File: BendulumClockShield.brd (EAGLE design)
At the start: 53.3 x 59.7 mm, 25 parts, among them J1 Cold Start, P1 Clock, P2 IR Recv, P3 Coil, P4 Batt, P5 Pwr, U1 LP2951-N

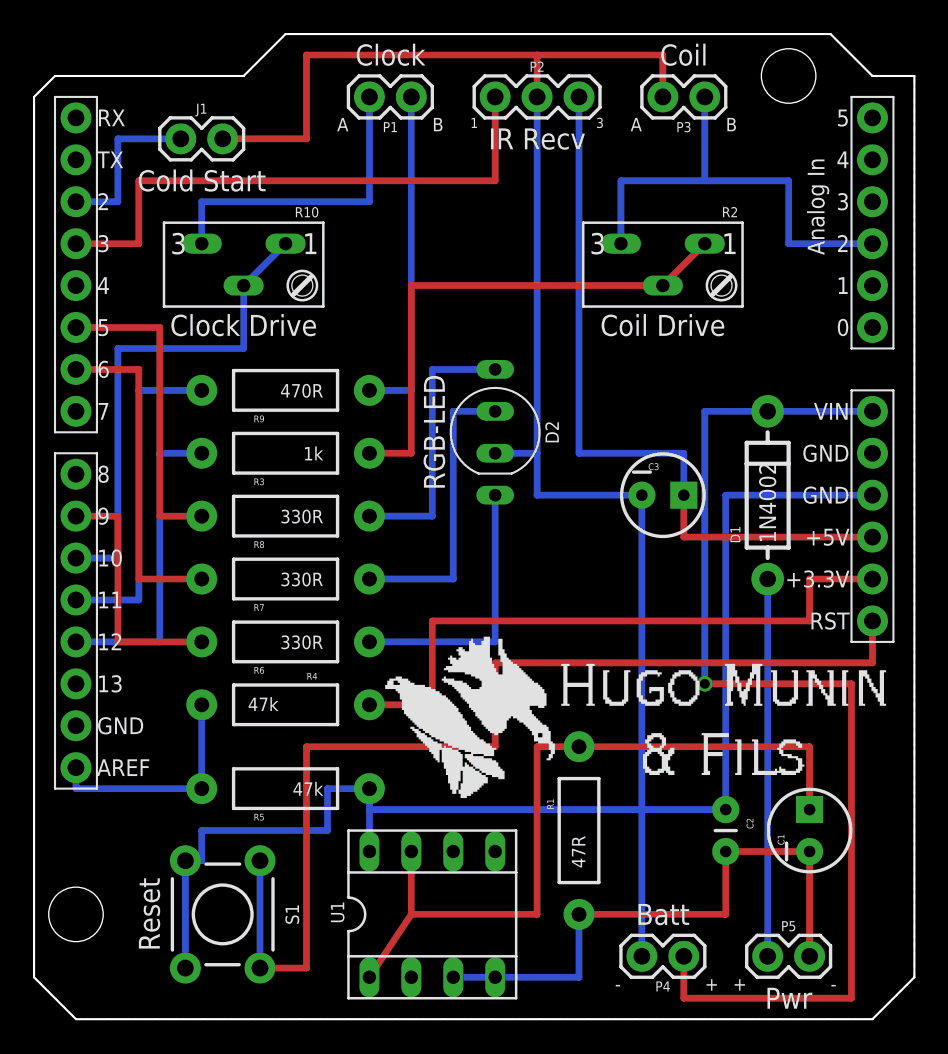
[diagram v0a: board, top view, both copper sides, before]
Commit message: Update to Rev G
Increase current drive to 68mA; 42mA for the Arduino and 26mA to keep
the the battery pack fully charged. (26mA is 0.01C for 2500mAh
batteries.)
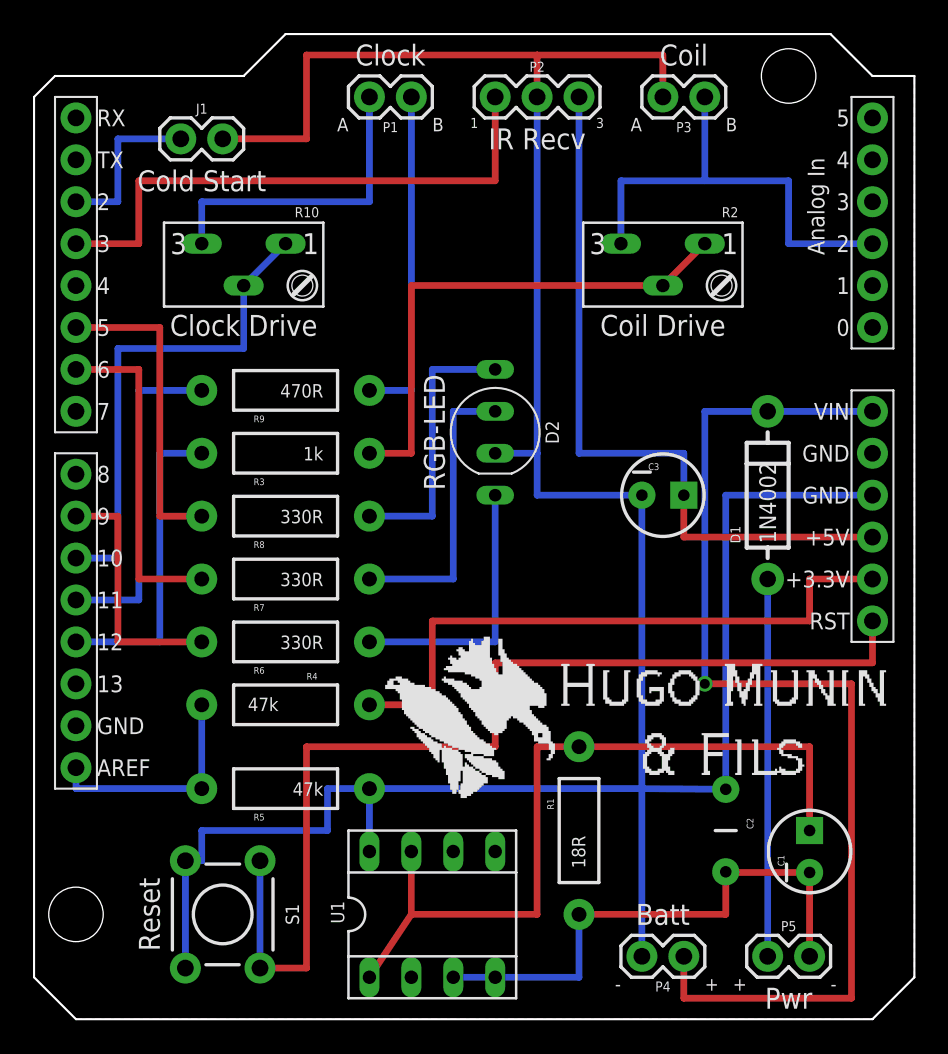
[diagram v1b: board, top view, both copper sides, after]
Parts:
- C2: device SparkFun-Capacitors:CAP-PTH-SMALL -> SparkFun-Capacitors:CAP-PTH-5MM
- R1: value 47R -> 18R
- moved C1 1.27 mm to (47.0, 10.2)
- moved C2 1.27 mm to (41.9, 11.4)
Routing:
- net N$3: track 35.6 -> 33.1 mm
- net U1: track 46.5 -> 47.8 mm
- net GND: track 173.2 -> 171.9 mm
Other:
- board text added: "Bendulum Clock Shield - Rev G"
- board text removed: "Bendulum Clock Shield - Rev F"
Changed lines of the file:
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@@
 <layer number="18" name="Vias" color="2" fill="1" visible="yes" active="yes"/>
 <layer number="19" name="Unrouted" color="6" fill="1" visible="yes" active="yes"/>
-<layer number="20" name="Dimension" color="15" fill="1" visible="yes" active="yes"/>
+<layer number="20" name="Dimension" color="15" fill="1" visible="no" active="yes"/>
 <layer number="21" name="tPlace" color="7" fill="1" visible="yes" active="yes"/>
 <layer number="22" name="bPlace" color="7" fill="1" visible="yes" active="yes"/>
-<layer number="23" name="tOrigins" color="15" fill="1" visible="yes" active="yes"/>
-<layer number="24" name="bOrigins" color="15" fill="1" visible="yes" active="yes"/>
+<layer number="23" name="tOrigins" color="15" fill="1" visible="no" active="yes"/>
+<layer number="24" name="bOrigins" color="15" fill="1" visible="no" active="yes"/>
 <layer number="25" name="tNames" color="7" fill="1" visible="yes" active="yes"/>
-<layer number="26" name="bNames" color="7" fill="1" visible="yes" active="yes"/>
+<layer number="26" name="bNames" color="7" fill="1" visible="no" active="yes"/>
 <layer number="27" name="tValues" color="7" fill="1" visible="no" active="yes"/>
 <layer number="28" name="bValues" color="7" fill="1" visible="no" active="yes"/>
@@
 <layer number="109" name="ref-old" color="11" fill="1" visible="no" active="yes"/>
 <layer number="116" name="Patch_BOT" color="9" fill="4" visible="no" active="yes"/>
-<layer number="121" name="_tsilk" color="7" fill="1" visible="yes" active="yes"/>
+<layer number="121" name="_tsilk" color="7" fill="1" visible="no" active="yes"/>
 <layer number="122" name="_bsilk" color="7" fill="1" visible="yes" active="yes"/>
 <layer number="125" name="_tNames" color="7" fill="1" visible="no" active="yes"/>
@@
 <board>
 <plain>
-<text x="40.64" y="24.13" size="1.778" layer="122" rot="MR0">Bendulum Clock
-Shield - Rev F</text>
+<text x="43.18" y="24.13" size="1.778" layer="122" font="vector" rot="MR0">Bendulum Clock
+Shield - Rev G</text>
 <text x="38.1" y="41.402" size="1.27" layer="121" align="bottom-center">Coil Drive</text>
 <text x="12.7" y="41.402" size="1.27" layer="121" align="bottom-center">Clock Drive</text>
@@
 <element name="P1" library="dehne" package="1X02" value="Clock" x="22.86" y="55.88" rot="R180"/>
 <element name="D1" library="SparkFun-DiscreteSemi" package="DIODE-1N4001-KIT" value="1N4002" x="44.45" y="31.75" rot="R90"/>
-<element name="C1" library="SparkFun-Capacitors" package="CPOL-RADIAL-10UF-25V" value="10uF" x="46.99" y="11.43" rot="R90">
-<attribute name="PROD_ID" value="CAP-08440" x="121.92" y="35.56" size="1.778" layer="27" rot="R90" display="off"/>
+<element name="C1" library="SparkFun-Capacitors" package="CPOL-RADIAL-10UF-25V" value="10uF" x="46.99" y="10.16" rot="R90">
+<attribute name="PROD_ID" value="CAP-08440" x="121.92" y="34.29" size="1.778" layer="27" rot="R90" display="off"/>
 </element>
-<element name="C2" library="SparkFun-Capacitors" package="CAP-PTH-SMALL" value="0.1uF" x="41.91" y="12.7" rot="R270"/>
+<element name="C2" library="SparkFun-Capacitors" package="CAP-PTH-5MM" value="0.1uF" x="41.91" y="11.43" rot="R270"/>
 <element name="P2" library="dehne" package="1X03" value="IR Recv" x="27.94" y="55.88"/>
 <element name="C3" library="SparkFun-Capacitors" package="CPOL-RADIAL-10UF-25V" value="47uF" x="38.1" y="31.75">
@@
 <element name="S1" library="dehne" package="TACTILE-PTH" value="Reset" x="11.43" y="6.35" rot="R270"/>
 <element name="U$2" library="dehne" package="HMF-LOGO" value="" x="38.1" y="17.78"/>
-<element name="R1" library="dehne" package="AXIAL-0.4" value="47R" x="33.02" y="11.43" rot="R90"/>
+<element name="R1" library="dehne" package="AXIAL-0.4" value="18R" x="33.02" y="11.43" rot="R90"/>
 <element name="R3" library="dehne" package="AXIAL-0.4" value="1k" x="15.24" y="34.29" rot="R180"/>
 <element name="R4" library="dehne" package="AXIAL-0.4" value="47k" x="15.24" y="19.05"/>
@@
 <contactref element="C1" pad="2"/>
 <contactref element="C2" pad="2"/>
-<wire x1="41.91" y1="6.35" x2="41.91" y2="10.16" width="0.4064" layer="1"/>
-<wire x1="41.91" y1="10.16" x2="46.99" y2="10.16" width="0.4064" layer="1"/>
-<wire x1="46.99" y1="3.81" x2="46.99" y2="10.16" width="0.4064" layer="1"/>
+<wire x1="41.91" y1="6.35" x2="41.91" y2="8.89" width="0.4064" layer="1"/>
+<wire x1="46.99" y1="3.81" x2="46.99" y2="8.89" width="0.4064" layer="1"/>
 <contactref element="R1" pad="P$1"/>
 <wire x1="33.02" y1="6.35" x2="33.02" y2="2.54" width="0.4064" layer="16"/>
@@
 <wire x1="33.02" y1="2.54" x2="27.94" y2="2.54" width="0.4064" layer="16"/>
 <wire x1="27.94" y1="2.54" x2="25.4" y2="2.54" width="0.4064" layer="16"/>
+<wire x1="46.99" y1="8.89" x2="41.91" y2="8.89" width="0.4064" layer="1"/>
+<wire x1="41.91" y1="8.89" x2="41.91" y2="8.93" width="0.4064" layer="1"/>
 </signal>
 <signal name="U1">
 <contactref element="C1" pad="1"/>
-<wire x1="46.99" y1="16.51" x2="46.99" y2="12.7" width="0.4064" layer="1"/>
+<wire x1="46.99" y1="16.51" x2="46.99" y2="11.43" width="0.4064" layer="1"/>
 <contactref element="R1" pad="P$2"/>
 <wire x1="46.99" y1="16.51" x2="33.02" y2="16.51" width="0.4064" layer="1"/>
@@
 <contactref element="U$1" pad="GND@0"/>
 <wire x1="50.8" y1="31.75" x2="41.91" y2="31.75" width="0.4064" layer="16"/>
-<wire x1="41.91" y1="31.75" x2="41.91" y2="12.7" width="0.4064" layer="16"/>
-<wire x1="36.83" y1="31.75" x2="36.83" y2="12.7" width="0.4064" layer="16"/>
-<wire x1="36.83" y1="3.81" x2="36.83" y2="12.7" width="0.4064" layer="16"/>
+<wire x1="41.91" y1="31.75" x2="41.91" y2="13.93" width="0.4064" layer="16"/>
+<wire x1="36.83" y1="31.75" x2="36.83" y2="13.97" width="0.4064" layer="16"/>
+<wire x1="36.83" y1="3.81" x2="36.83" y2="13.97" width="0.4064" layer="16"/>
 <wire x1="36.83" y1="31.75" x2="30.48" y2="31.75" width="0.4064" layer="16"/>
 <wire x1="30.48" y1="31.75" x2="30.48" y2="34.29" width="0.4064" layer="16"/>
@@
 <vertex x="0" y="55.88"/>
 </polygon>
-<wire x1="41.91" y1="12.7" x2="36.83" y2="12.7" width="0.4064" layer="16"/>
+<wire x1="41.91" y1="13.93" x2="36.83" y2="13.97" width="0.4064" layer="16"/>
 <contactref element="R5" pad="P$1"/>
 <contactref element="U1" pad="8"/>
-<wire x1="20.32" y1="10.16" x2="20.32" y2="12.7" width="0.4064" layer="16"/>
-<wire x1="20.32" y1="12.7" x2="20.32" y2="13.97" width="0.4064" layer="16"/>
-<wire x1="36.83" y1="12.7" x2="20.32" y2="12.7" width="0.4064" layer="16"/>
+<wire x1="20.32" y1="10.16" x2="20.32" y2="13.97" width="0.4064" layer="16"/>
+<wire x1="36.83" y1="13.97" x2="20.32" y2="13.97" width="0.4064" layer="16"/>
 <contactref element="S1" pad="3"/>
 <wire x1="9.1694" y1="9.6012" x2="10.16" y2="9.6012" width="0.4064" layer="16"/>

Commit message: Update to Rev H
Add header for TMP-102 temperature sensor
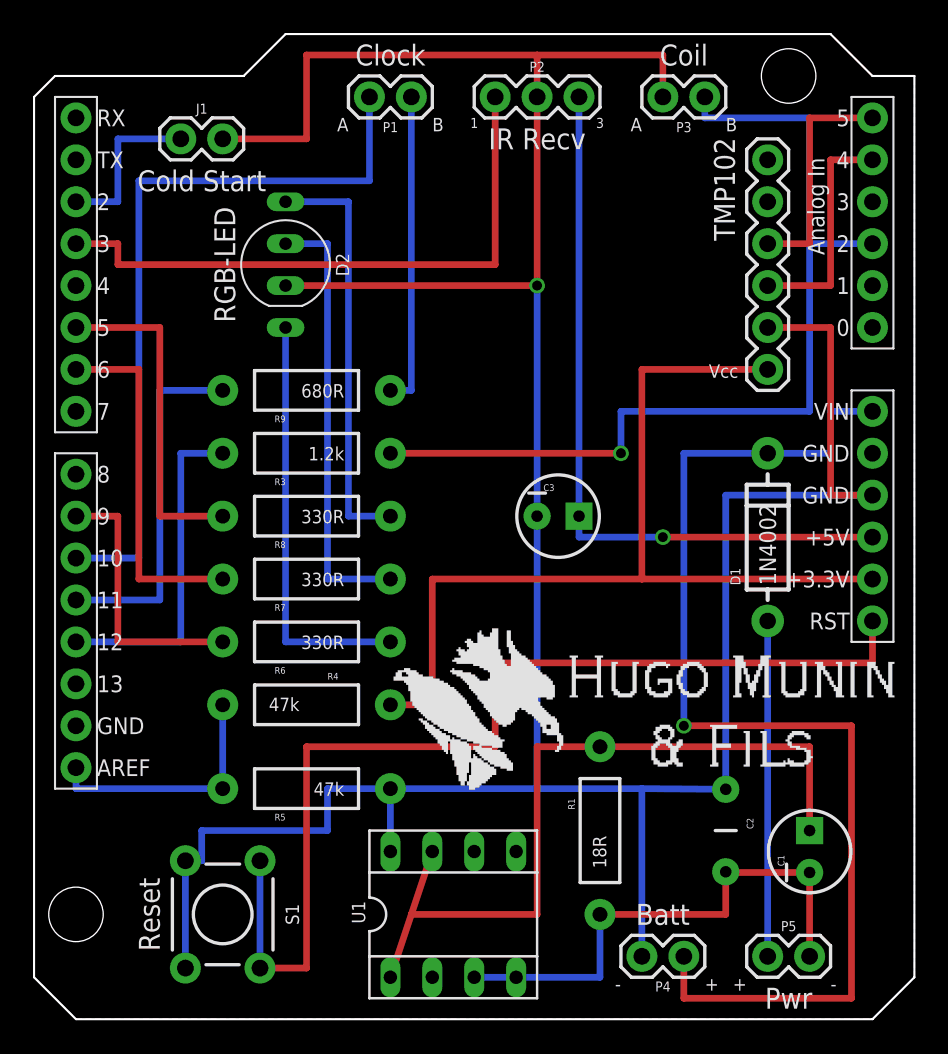
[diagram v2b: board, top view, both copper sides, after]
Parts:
- removed R10, R2: 500R, dehne:S64Y
- added TMP102: P6, dehne:1X06
- R3: value 1k -> 1.2k
- R9: value 470R -> 680R
- moved D2 16.3 mm to (15.2, 45.7)
- moved C3 6.48 mm to (31.8, 30.5)
- moved D1 2.54 mm to (44.5, 29.2)
- moved R3 1.27 mm to (16.5, 34.3)
- moved R4 1.27 mm to (16.5, 19.1)
- moved R5 1.27 mm to (16.5, 14.0)
- moved R6 1.27 mm to (16.5, 22.9)
- moved R7 1.27 mm to (16.5, 26.7)
- moved R8 1.27 mm to (16.5, 30.5)
- moved R9 1.27 mm to (16.5, 38.1)
- moved U1 1.27 mm to (25.4, 6.35)
- moved R1 1.27 mm to (34.3, 11.4)
- moved U$2 0.72 mm to (38.6, 18.3)
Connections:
- removed net N$20: P1.2, R10.3
- new net N$16: TMP102.3, U$1.A5
- net GND: now also TMP102.5
- net N$21: now also P1.2; no longer R10.1, R10.2
- net N$6: now also R3.P$1; no longer R2.3
- net N$7: now also TMP102.6
- net N$9: now also TMP102.4, U$1.A4; no longer R2.1, R2.2, R3.P$1
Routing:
- net N$6: track 27.9 -> 57.2 mm, vias 0 -> 1
- net GND: track 171.9 -> 194.8 mm, vias 0 -> 1
- net N$7: track 38.1 -> 57.1 mm
- net N$20: track 19.1 -> 0.00 mm
- net N$9: track 31.5 -> 14.0 mm
- net N$21: track 30.3 -> 45.7 mm
- net N$16: track 0.00 -> 14.0 mm
- net N$18: track 17.8 -> 26.7 mm
- net N$19: track 16.5 -> 25.4 mm
- net N$17: track 16.5 -> 25.4 mm
- net N$1: track 22.9 -> 20.3 mm
- net N$14: track 34.3 -> 36.8 mm
- net N$2: track 67.3 -> 69.8 mm
- net N$8: track 19.0 -> 20.3 mm
- net N$3: track 33.1 -> 31.8 mm
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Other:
- board text added: "Bendulum Clock Shield - Rev H"
- board text added: "Vcc"
- board text removed: "Bendulum Clock Shield - Rev G"
- board text removed: "Clock Drive"
- board text removed: "Coil Drive"
